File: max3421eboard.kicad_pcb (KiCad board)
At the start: 2 copper layers, 41.3 x 48.9 mm, 32 parts, among them J1 USB A, J2 USB MicroB, J3 1x10, J4 1x8, J5 1x8, J6 1x3, J7 Conn_01x04, U1 MAX3421E, U2 LP2985-3.3, U3 STMPS2141STR, Y1 12MHz

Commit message: Adjustments
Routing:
- net Net-(J4-Pad8): track 23.0 -> 19.6 mm
- net Net-(J4-Pad7): track 20.1 -> 19.0 mm
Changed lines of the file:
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@@
     (thickness 1.6)
     (drawings 47)
-    (tracks 458)
+    (tracks 461)
     (zones 0)
     (modules 32)
@@
     (46 B.CrtYd user)
     (47 F.CrtYd user)
-    (48 B.Fab user hide)
-    (49 F.Fab user hide)
+    (48 B.Fab user)
+    (49 F.Fab user)
   )
   (setup
@@
     (effects (font (size 1 1) (thickness 0.15)))
   )
-  (gr_circle (center 36.195 80.01) (end 36.495 80.01) (layer F.SilkS) (width 0.12))
+  (gr_circle (center 36.195 80.645) (end 36.395 80.645) (layer F.SilkS) (width 0.4))
   (gr_text U1 (at 36.83 76.835) (layer F.SilkS)
     (effects (font (size 1 1) (thickness 0.15)))
@@
   (segment (start 24.13 90.17) (end 23.495 90.17) (width 0.25) (layer F.Cu) (net 19))
   (segment (start 30.664991 82.983597) (end 32.368588 81.28) (width 0.25) (layer F.Cu) (net 19))
-  (segment (start 23.495 90.17) (end 25.4 90.17) (width 0.25) (layer F.Cu) (net 19))
-  (segment (start 30.66499 84.90501) (end 30.664991 82.983597) (width 0.25) (layer F.Cu) (net 19))
-  (segment (start 25.4 90.17) (end 30.66499 84.90501) (width 0.25) (layer F.Cu) (net 19))
   (segment (start 36.927689 79.407563) (end 34.241025 79.407563) (width 0.25) (layer F.Cu) (net 19))
   (segment (start 34.241025 79.407563) (end 32.059294 81.589294) (width 0.25) (layer F.Cu) (net 19))
-  (segment (start 29.21 92.71) (end 23.495 92.71) (width 0.25) (layer F.Cu) (net 20))
-  (segment (start 31.115 90.805) (end 29.21 92.71) (width 0.25) (layer F.Cu) (net 20))
-  (segment (start 31.115 83.169998) (end 31.115 90.805) (width 0.25) (layer F.Cu) (net 20))
+  (segment (start 30.664991 83.001419) (end 24.13141 89.535) (width 0.25) (layer F.Cu) (net 19))
+  (segment (start 30.664991 82.983597) (end 30.664991 83.001419) (width 0.25) (layer F.Cu) (net 19))
+  (segment (start 24.13 89.535) (end 23.495 90.17) (width 0.25) (layer F.Cu) (net 19))
+  (segment (start 24.13141 89.535) (end 24.13 89.535) (width 0.25) (layer F.Cu) (net 19))
   (segment (start 33.094999 81.189999) (end 31.115 83.169998) (width 0.25) (layer F.Cu) (net 20))
   (segment (start 36.235251 81.189999) (end 33.094999 81.189999) (width 0.25) (layer F.Cu) (net 20))
   (segment (start 36.927689 81.882437) (end 36.235251 81.189999) (width 0.25) (layer F.Cu) (net 20))
+  (segment (start 25.4 90.805) (end 23.495 92.71) (width 0.25) (layer F.Cu) (net 20))
+  (segment (start 25.4 89.535) (end 25.4 90.805) (width 0.25) (layer F.Cu) (net 20))
+  (segment (start 31.115 83.169998) (end 31.115 83.18782) (width 0.25) (layer F.Cu) (net 20))
+  (segment (start 31.115 83.18782) (end 25.4 88.90282) (width 0.25) (layer F.Cu) (net 20))
+  (segment (start 25.4 88.90282) (end 25.4 89.535) (width 0.25) (layer F.Cu) (net 20))
   (segment (start 43.815 86.36) (end 43.815 86.995) (width 0.25) (layer B.Cu) (net 21))
   (segment (start 43.815 86.995) (end 40.64 90.17) (width 0.25) (layer B.Cu) (net 21))

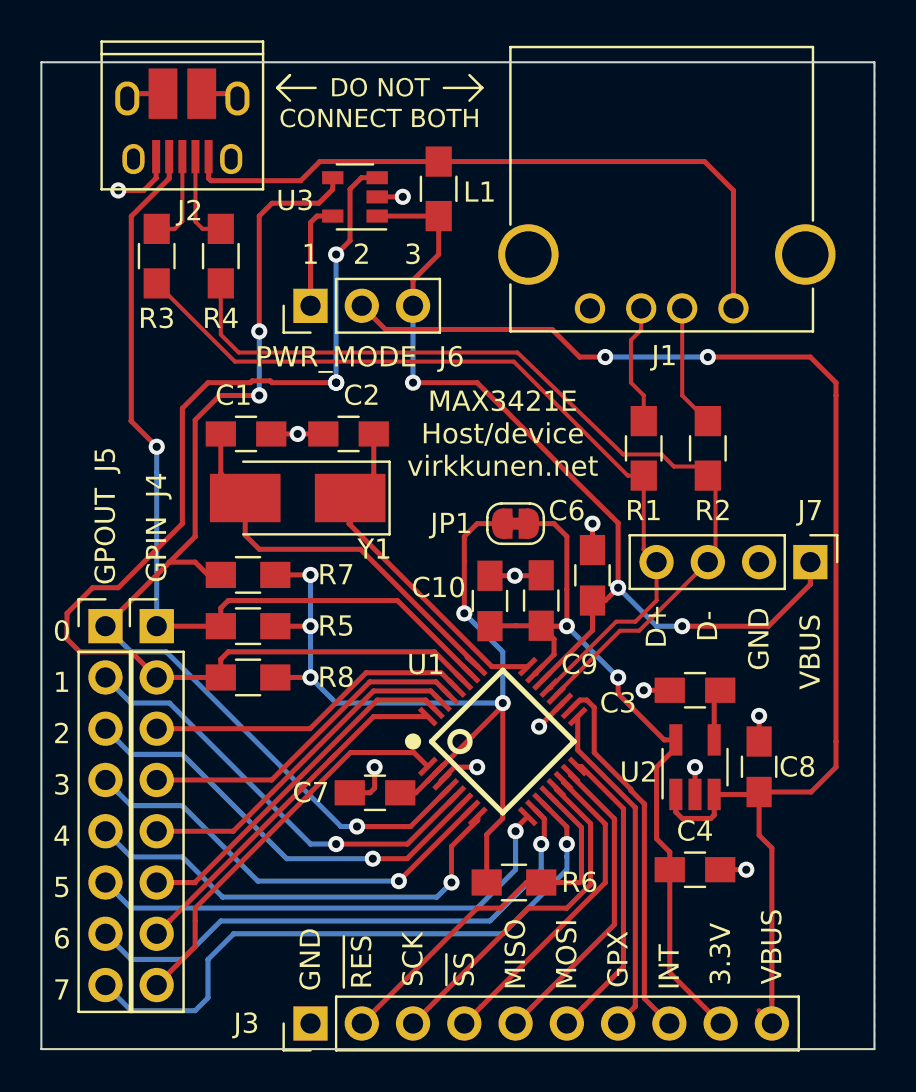
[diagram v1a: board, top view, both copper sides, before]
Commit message: Move decoupling capacitors around for better filtering
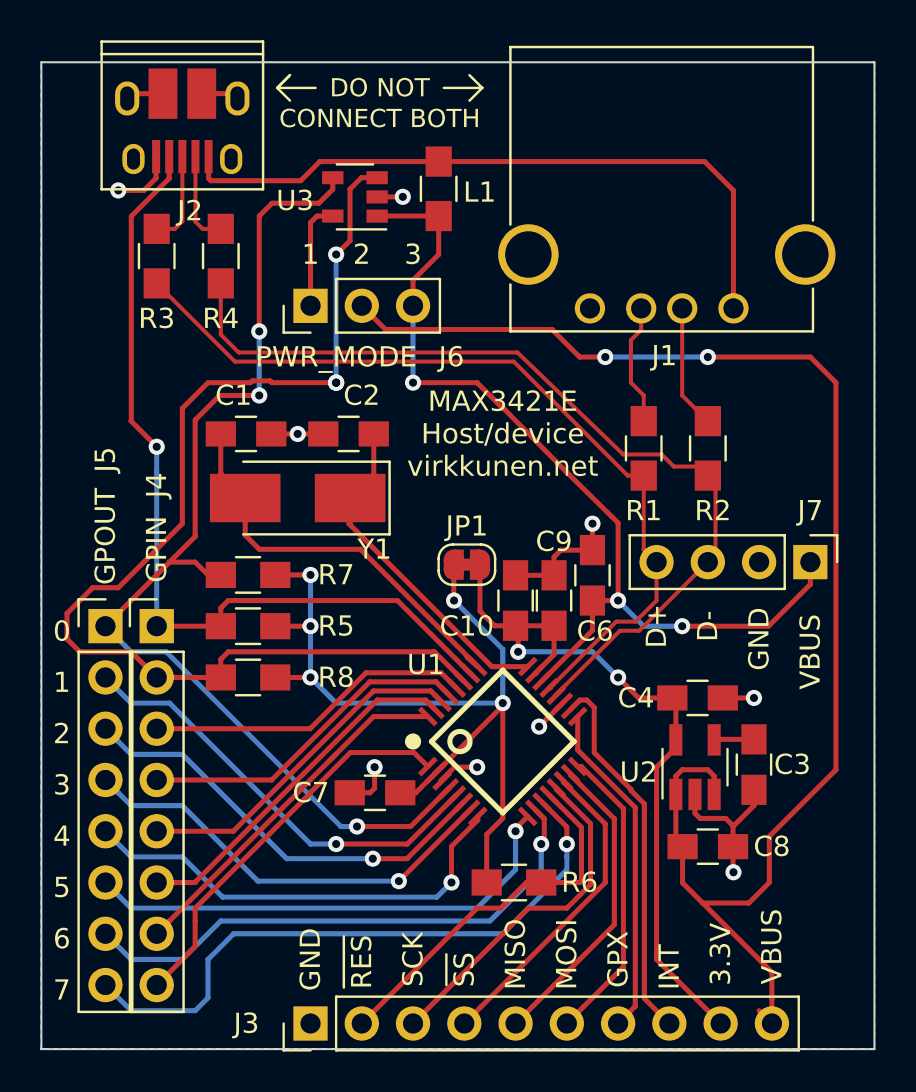
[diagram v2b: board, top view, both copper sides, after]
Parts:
- moved C4 8.51 mm to (50.3, 78.5)
- moved C8 4.70 mm to (50.8, 85.9), turned to 0 degrees
- moved C3 4.70 mm to (53.1, 81.8), turned to 270 degrees
- moved JP1 3.15 mm to (38.9, 71.9)
- moved C10 1.27 mm to (41.3, 73.7)
- moved C9 0.63 mm to (43.2, 73.7)
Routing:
- net GND: track 28.1 -> 34.4 mm, vias 12 -> 9
- net VBUS: track 67.4 -> 73.1 mm
- net VL: track 48.3 -> 45.0 mm
- net +3V3: track 37.5 -> 36.3 mm
- net Net-(C3-Pad1): track 2.58 -> 1.98 mm
